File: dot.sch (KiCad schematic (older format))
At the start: 34 parts

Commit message: Added a level shifter and removed a channel
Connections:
- net STRIP4: no longer names the net of U?.10 (IO25)
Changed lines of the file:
@@
 F17 "BUT_USER" O R 7550 4750 50
 F18 "STRIP3" I L 6600 4500 50
-F19 "STRIP4" I L 6600 4600 50
 $EndSheet
 $Comp
@@
 Text Label 6500 4500 2    50   ~ 0
 STRIP3
-Text Label 6500 4600 2    50   ~ 0
-STRIP4
-Wire Wire Line
-	6500 4600 6600 4600
 Wire Wire Line
 	6600 4500 6500 4500
@@
 Text Label 4250 4750 0    50   ~ 0
 STRIP3
-Text Label 4250 4850 0    50   ~ 0
-STRIP4
 Wire Wire Line
 	4250 4450 4150 4450
@@
 	4250 4750 4150 4750
 Wire Wire Line
-	4250 4850 4150 4850
-Wire Wire Line
 	4250 4350 4150 4350

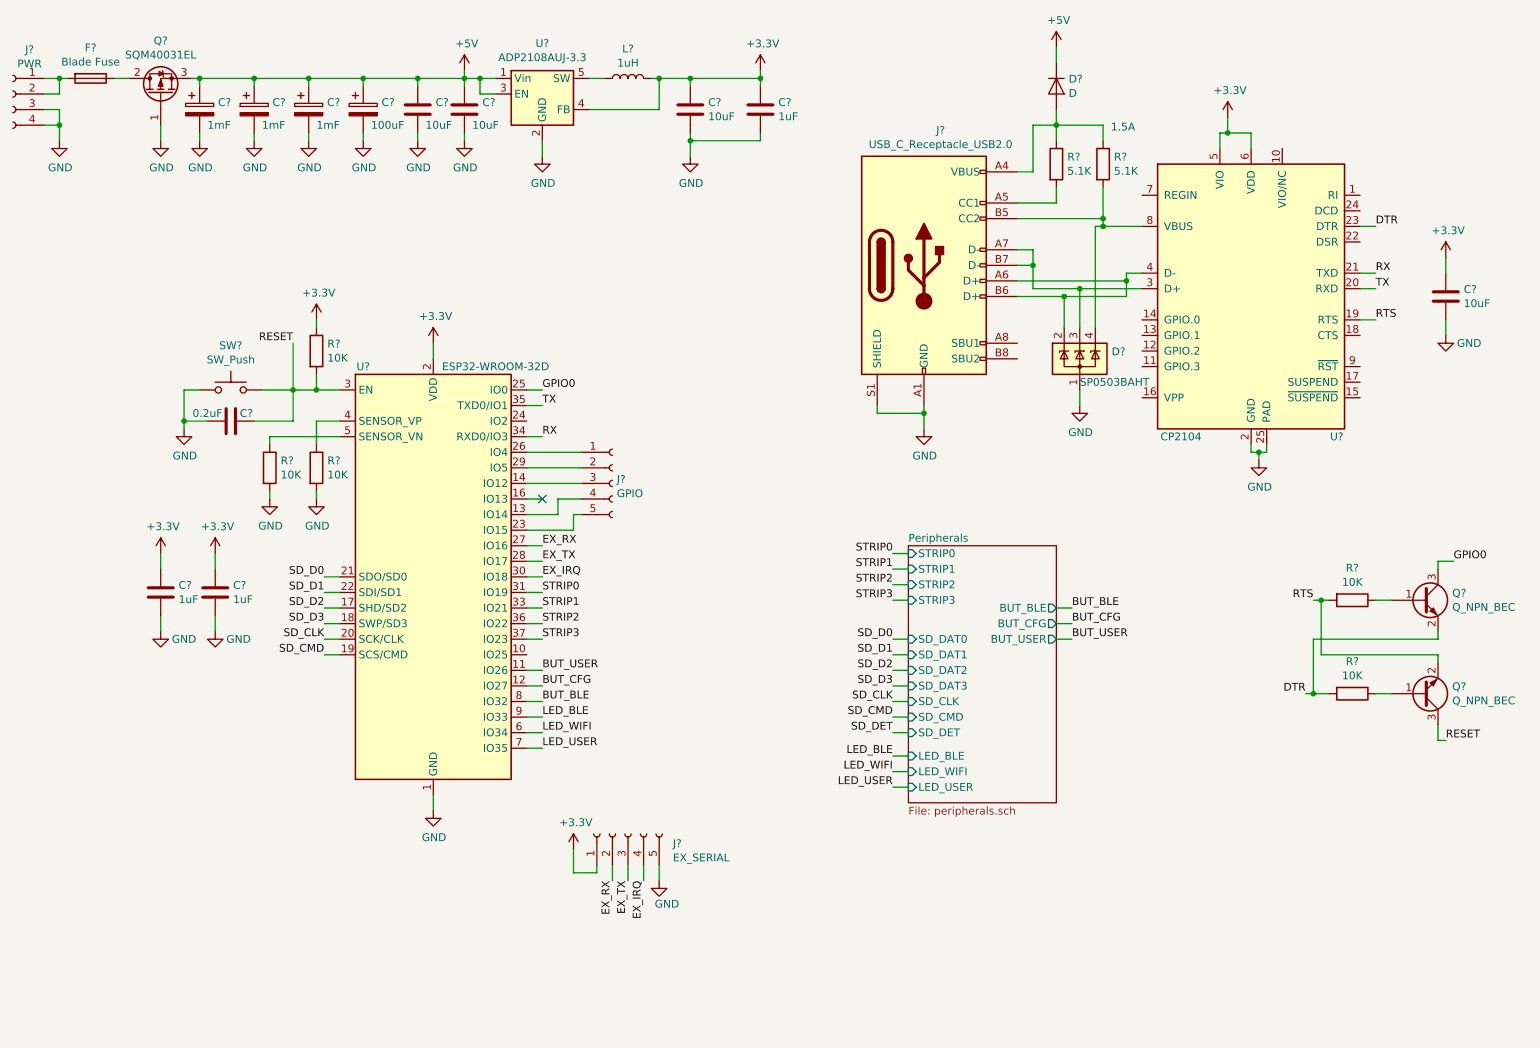
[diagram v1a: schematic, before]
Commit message: About to change the entire damn thing to handle more current
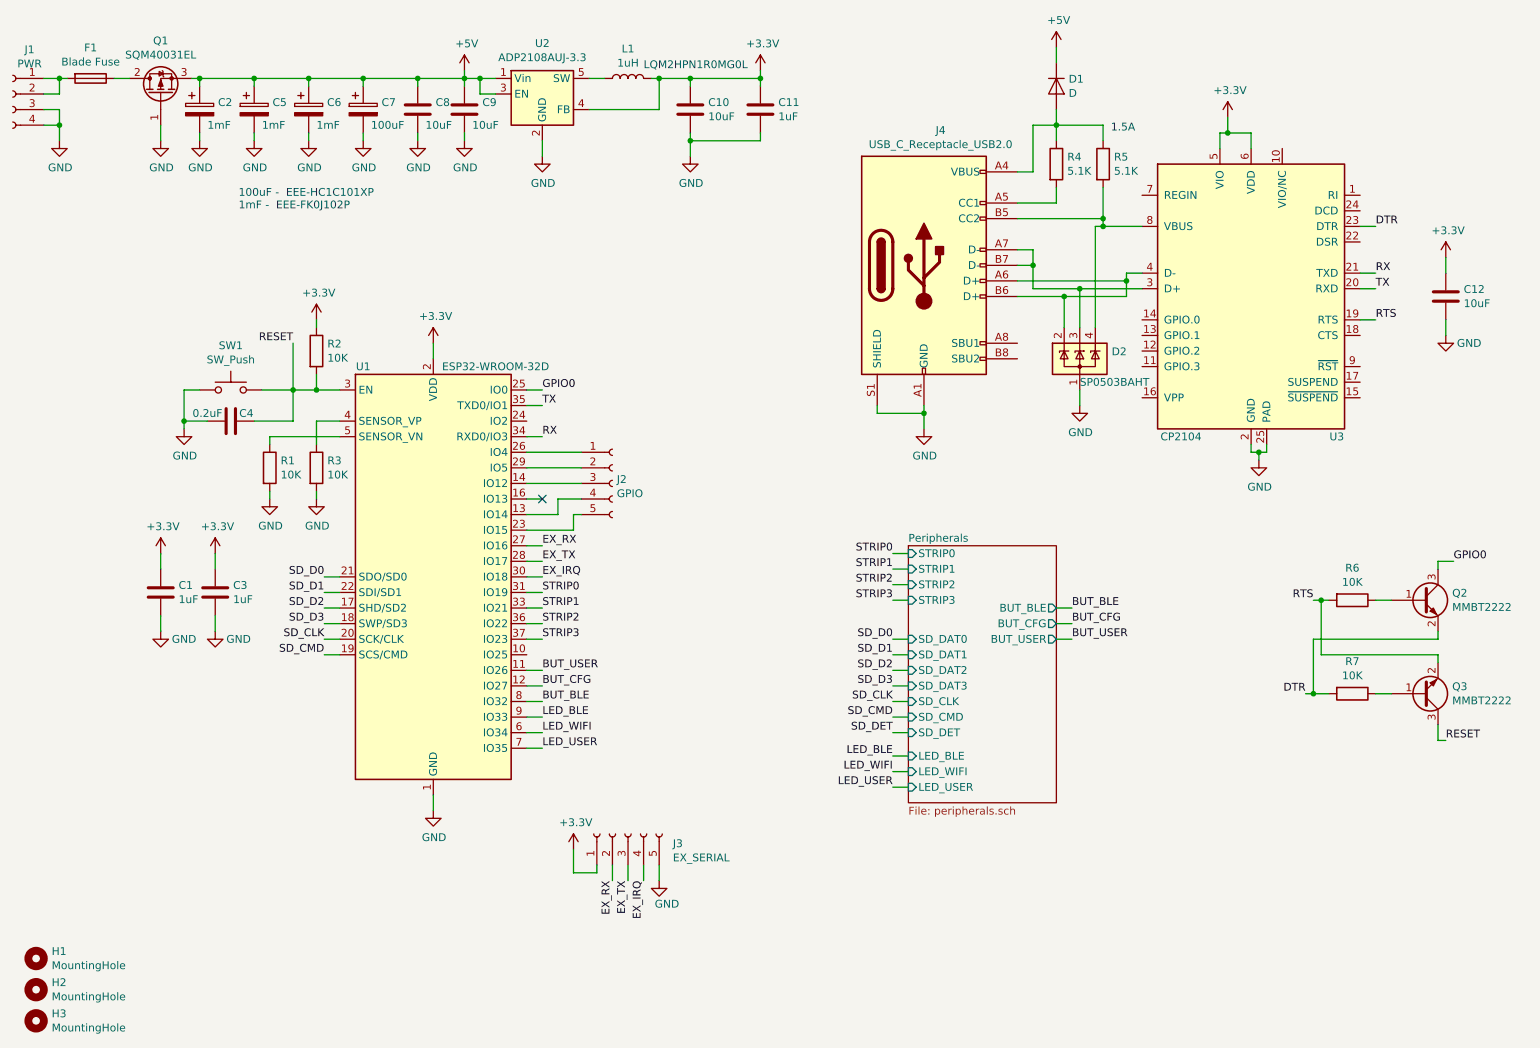
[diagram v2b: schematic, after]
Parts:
- added H1, H2, H3: MountingHole, MountingHole:MountingHole_2.5mm, symbol Mechanical:MountingHole
- C1, C10, C11, C12, C3, C4, C8, C9: renamed from C?; footprint (none) -> Capacitor_SMD:C_0805_2012Metric
- C2, C5, C6: renamed from C?; footprint (none) -> Capacitor_SMD:CP_Elec_8x10.5
- C7: renamed from C?; footprint (none) -> Capacitor_SMD:CP_Elec_6.3x3.9
- D1: renamed from D?; footprint (none) -> Diode_SMD:D_SOD-123F
- J2, J3: renamed from J?; footprint (none) -> Connector_PinHeader_2.54mm:PinHeader_1x05_P2.54mm_Vertical
- J4: renamed from J?; footprint (none) -> Connector_USB:USB_C_Receptacle_GCT_USB4085
- L1: renamed from L?; footprint (none) -> Inductor_SMD:L_1008_2520Metric
- Q2, Q3: renamed from Q?; value Q_NPN_BEC -> MMBT2222; footprint (none) -> Package_TO_SOT_SMD:SOT-23
- R1, R2, R3, R4, R5, R6, R7: renamed from R?; footprint (none) -> Resistor_SMD:R_0805_2012Metric
- SW1: renamed from SW?; footprint (none) -> Button_Switch_SMD:SW_Push_1P1T_NO_CK_KMR2
- gave numbers to parts that had none: 7
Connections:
- net GND: now also SW1.2; no longer SW1.1
- net RESET: now also SW1.1; no longer SW1.2
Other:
- note added: "100uF - EEE-HC1C101XP \n1mF - EEE-FK0J102P"
- note added: "LQM2HPN1R0MG0L"

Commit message: Ordered files
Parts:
- removed J3: EX_SERIAL, Connector_PinHeader_2.54mm:PinHeader_1x05_P2.54mm_Vertical, symbol Connector:Conn_01x05_Female
- removed U3: CP2104, Package_DFN_QFN:QFN-24-1EP_4x4mm_P0.5mm_EP2.6x2.6mm, symbol Interface_USB:CP2104
- added U3: CH340T, Package_SO:SSOP-20_5.3x7.2mm_P0.65mm, symbol Interface_USB:CH340T
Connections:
- net +3V3: now also U3.19 (VCC), U3.5 (V3)
- net DTR: now also U3.15 (~DTR)
- net GND: now also J1.1 (Pin_1), J1.2 (Pin_2), U3.8 (GND); no longer J1.3 (Pin_3), J1.4 (Pin_4)
- net RTS: now also U3.16 (~RTS)
- net RX: now also U3.3 (TXD)
- net STRIP0: now also U1.10 (IO25); no longer U1.31 (IO19)
- net STRIP1: now also U1.37 (IO23); no longer U1.33 (IO21)
- net STRIP3: now also U1.33 (IO21); no longer U1.37 (IO23)
- net TX: now also U3.4 (RXD)
- net at D2.2 (K), J4.A6 (D+), J4.B6 (D+): now also U3.6 (UD+)
- net at D2.3 (K), J4.A7 (D-), J4.B7 (D-): now also U3.7 (UD-)
- net EX_IRQ renamed STRIP5
- net EX_RX renamed STRIP7
- net EX_TX renamed STRIP6
- new net: F1.2, J1.3 (Pin_3), J1.4 (Pin_4)
- new net STRIP4: U1.31 (IO19)
